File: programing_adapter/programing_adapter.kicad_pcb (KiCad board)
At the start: 2 copper layers, 87 x 98 mm, 72 parts, among them J1 Conn_02x05_SWD, J2 USB_A, SW1 SW_RESET

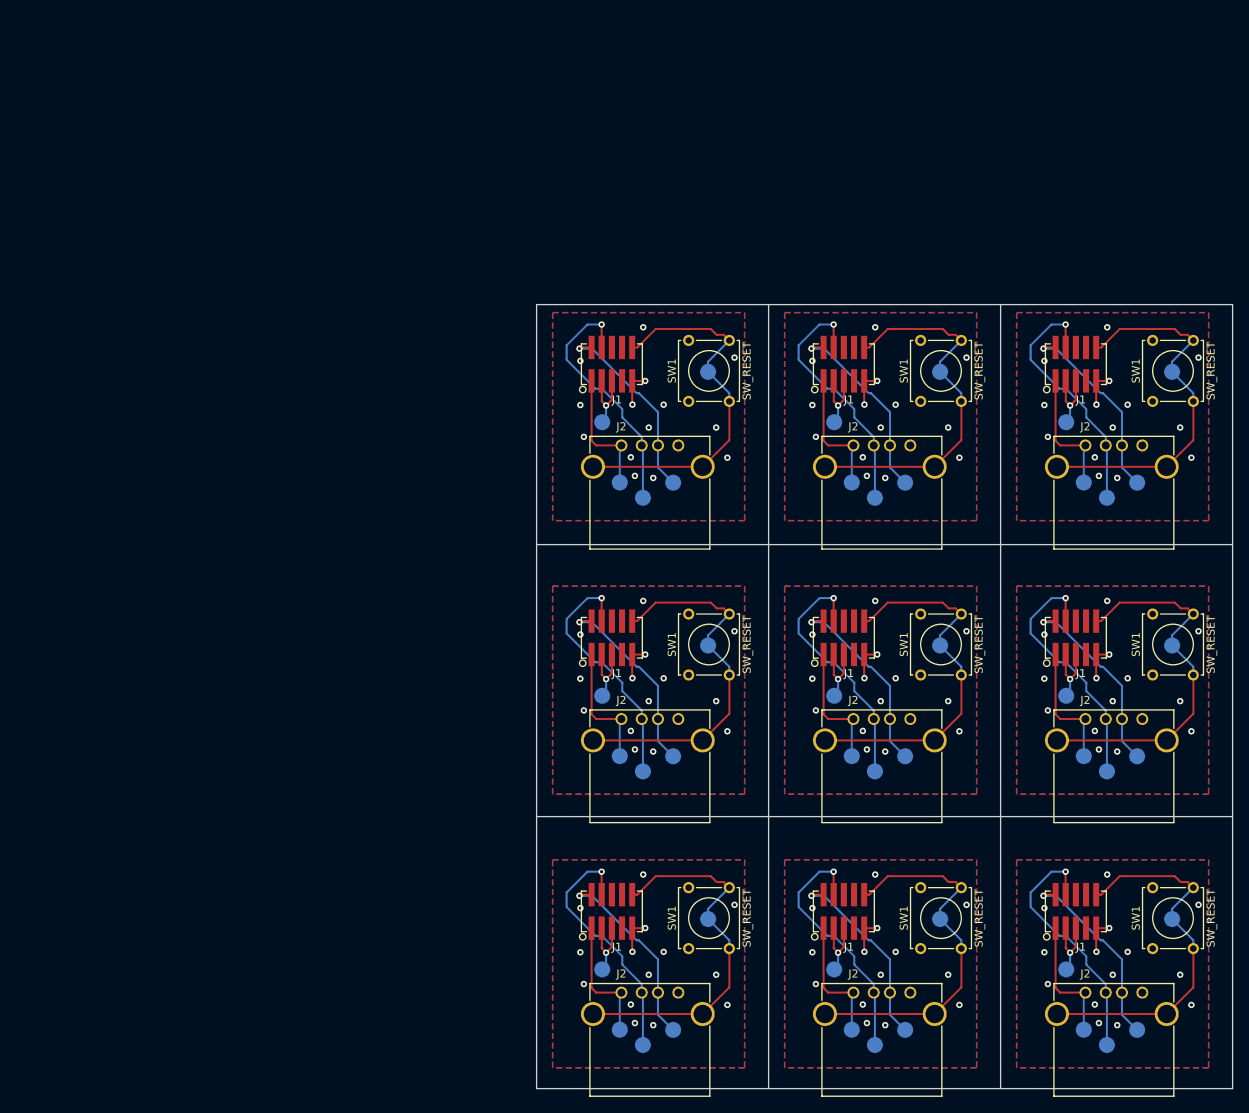
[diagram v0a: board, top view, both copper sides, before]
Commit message: remake programming adapter to be much more flexable
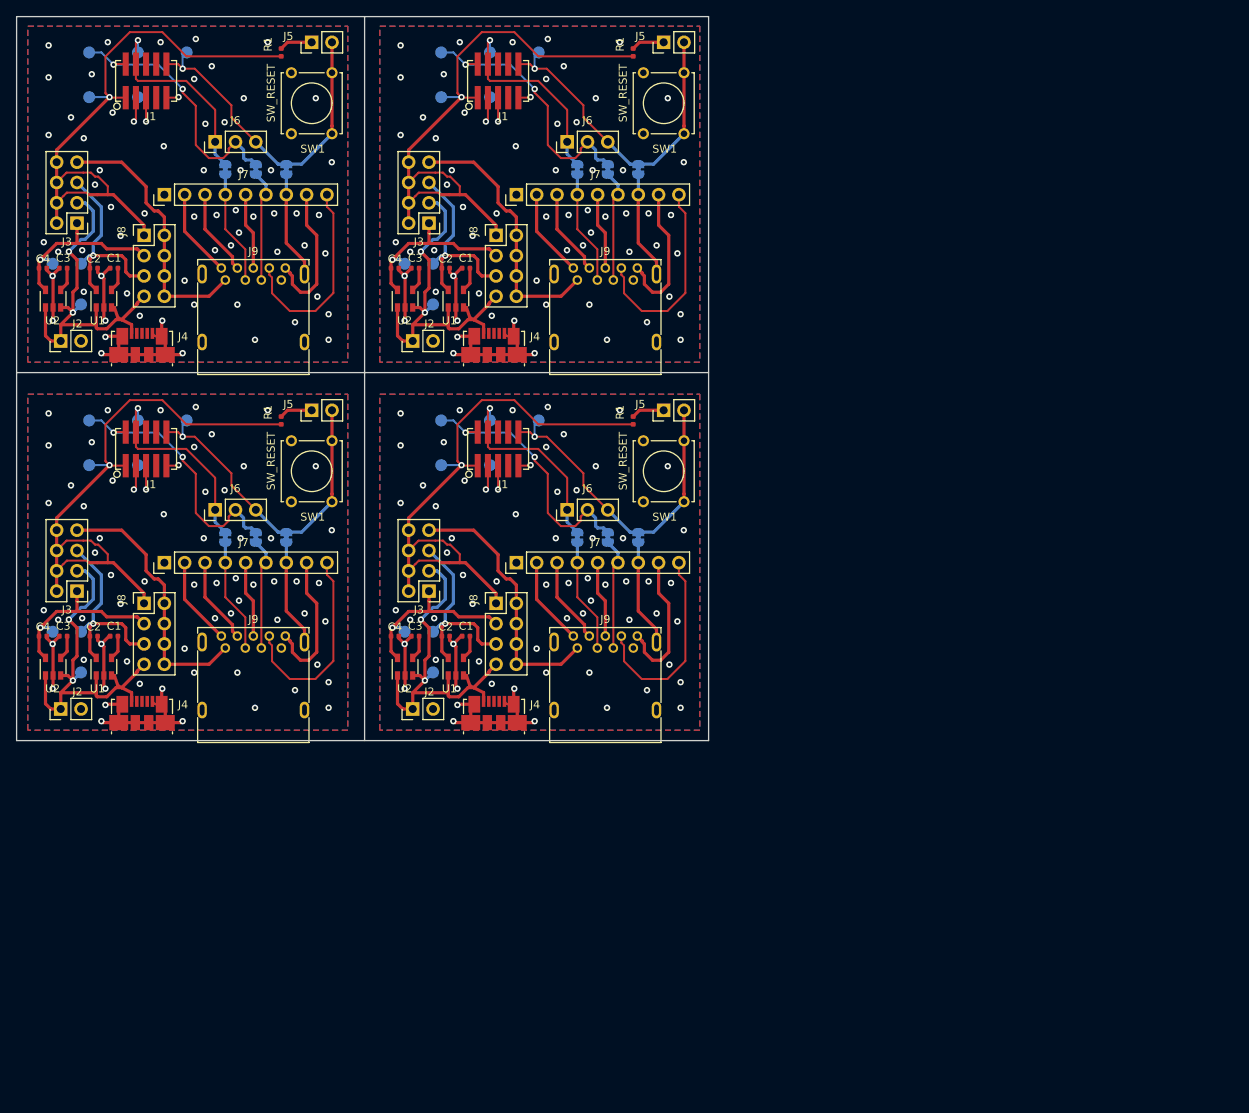
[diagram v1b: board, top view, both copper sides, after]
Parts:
- removed the J1 at (186.4, 148.8)
- removed the J1 at (157.4, 148.8)
- removed the J1 at (128.4, 148.8)
- removed the J1 at (186.4, 114.7)
- removed the J1 at (157.4, 114.7)
- removed the J1 at (128.4, 114.7)
- removed the J1 at (186.4, 80.5)
- removed the J1 at (157.4, 80.5)
- removed the J1 at (128.4, 80.5)
- removed the J2 at (187.6, 159.0)
- removed the J2 at (158.6, 159.0)
- removed the J2 at (129.6, 159.0)
- removed the J2 at (187.6, 124.8)
- removed the J2 at (158.6, 124.8)
- removed the J2 at (129.6, 124.8)
- removed the J2 at (187.6, 90.6)
- removed the J2 at (158.6, 90.6)
- removed the J2 at (129.6, 90.6)
- removed the SW1 at (196.0, 153.5)
- removed the SW1 at (167.0, 153.5)
- removed the SW1 at (138.0, 153.5)
- removed the SW1 at (196.0, 119.3)
- removed the SW1 at (167.0, 119.3)
- removed the SW1 at (138.0, 119.3)
- removed the SW1 at (196.0, 85.1)
- removed the SW1 at (167.0, 85.1)
- removed the SW1 at (138.0, 85.1)
- removed the TP1 at (187.4, 163.6)
- removed the TP1 at (158.4, 163.6)
- removed the TP1 at (129.4, 163.6)
- removed the TP1 at (187.4, 129.4)
- removed the TP1 at (158.4, 129.4)
- removed the TP1 at (129.4, 129.4)
- removed the TP1 at (187.4, 95.2)
- removed the TP1 at (158.4, 95.2)
- removed the TP1 at (129.4, 95.2)
- removed the TP2 at (185.2, 156.1)
- removed the TP2 at (156.2, 156.1)
- removed the TP2 at (127.2, 156.1)
- removed the TP2 at (185.2, 121.9)
- removed the TP2 at (156.2, 121.9)
- removed the TP2 at (127.2, 121.9)
- removed the TP2 at (185.2, 87.7)
- removed the TP2 at (156.2, 87.7)
- removed the TP2 at (127.2, 87.7)
- removed the TP3 at (194.1, 163.7)
- removed the TP3 at (165.1, 163.7)
- removed the TP3 at (136.1, 163.7)
- removed the TP3 at (194.1, 129.5)
- removed the TP3 at (165.1, 129.5)
- removed the TP3 at (136.1, 129.5)
- removed the TP3 at (194.1, 95.3)
- removed the TP3 at (165.1, 95.3)
- removed the TP3 at (136.1, 95.3)
- removed the TP4 at (190.3, 165.6)
- removed the TP4 at (161.3, 165.6)
- removed the TP4 at (132.3, 165.6)
- removed the TP4 at (190.3, 131.3)
- removed the TP4 at (161.3, 131.3)
- removed the TP4 at (132.3, 131.3)
- removed the TP4 at (190.3, 97.2)
- removed the TP4 at (161.3, 97.2)
- removed the TP4 at (132.3, 97.2)
- removed the TP5 at (198.4, 149.8)
- removed the TP5 at (169.4, 149.8)
- removed the TP5 at (140.4, 149.8)
- removed the TP5 at (198.4, 115.6)
- removed the TP5 at (169.4, 115.6)
- removed the TP5 at (140.4, 115.6)
- removed the TP5 at (198.4, 81.4)
- removed the TP5 at (169.4, 81.4)
- removed the TP5 at (140.4, 81.4)
- added C1: .1u, Capacitor_SMD:C_0402_1005Metric, F.Cu at (110.2, 114.4)
- added C1: .1u, Capacitor_SMD:C_0402_1005Metric, F.Cu at (66.2, 114.4)
- added C1: .1u, Capacitor_SMD:C_0402_1005Metric, F.Cu at (110.2, 68.4)
- added C1: .1u, Capacitor_SMD:C_0402_1005Metric, F.Cu at (66.2, 68.4)
- added C2: 4.7u, Capacitor_SMD:C_0402_1005Metric, F.Cu at (107.6, 114.4)
- added C2: 4.7u, Capacitor_SMD:C_0402_1005Metric, F.Cu at (63.6, 114.4)
- added C2: 4.7u, Capacitor_SMD:C_0402_1005Metric, F.Cu at (107.6, 68.4)
- added C2: 4.7u, Capacitor_SMD:C_0402_1005Metric, F.Cu at (63.6, 68.4)
- added C3: .1u, Capacitor_SMD:C_0402_1005Metric, F.Cu at (103.8, 114.4)
- added C3: .1u, Capacitor_SMD:C_0402_1005Metric, F.Cu at (59.8, 114.4)
- added C3: .1u, Capacitor_SMD:C_0402_1005Metric, F.Cu at (103.8, 68.4)
- added C3: .1u, Capacitor_SMD:C_0402_1005Metric, F.Cu at (59.8, 68.4)
- added C4: 4.7u, Capacitor_SMD:C_0402_1005Metric, F.Cu at (101.3, 114.4)
- added C4: 4.7u, Capacitor_SMD:C_0402_1005Metric, F.Cu at (57.3, 114.4)
- added C4: 4.7u, Capacitor_SMD:C_0402_1005Metric, F.Cu at (101.3, 68.4)
- added C4: 4.7u, Capacitor_SMD:C_0402_1005Metric, F.Cu at (57.3, 68.4)
- added J1: SWD, CustomKiCadLibrary:185G087, F.Cu at (114.2, 91.0)
- added J1: SWD, CustomKiCadLibrary:185G087, F.Cu at (70.2, 91.0)
- added J1: SWD, CustomKiCadLibrary:185G087, F.Cu at (114.2, 45.0)
- added J1: SWD, CustomKiCadLibrary:185G087, F.Cu at (70.2, 45.0)
- added J2: Vin, Connector_PinHeader_2.54mm:PinHeader_1x02_P2.54mm_Vertical, F.Cu at (103.5, 123.5)
- added J2: Vin, Connector_PinHeader_2.54mm:PinHeader_1x02_P2.54mm_Vertical, F.Cu at (59.5, 123.5)
- added J2: Vin, Connector_PinHeader_2.54mm:PinHeader_1x02_P2.54mm_Vertical, F.Cu at (103.5, 77.5)
- added J2: Vin, Connector_PinHeader_2.54mm:PinHeader_1x02_P2.54mm_Vertical, F.Cu at (59.5, 77.5)
- added J3: Set Prog V, Connector_PinHeader_2.54mm:PinHeader_2x04_P2.54mm_Vertical, F.Cu at (105.5, 108.8)
- added J3: Set Prog V, Connector_PinHeader_2.54mm:PinHeader_2x04_P2.54mm_Vertical, F.Cu at (61.5, 108.8)
- added J3: Set Prog V, Connector_PinHeader_2.54mm:PinHeader_2x04_P2.54mm_Vertical, F.Cu at (105.5, 62.8)
- added J3: Set Prog V, Connector_PinHeader_2.54mm:PinHeader_2x04_P2.54mm_Vertical, F.Cu at (61.5, 62.8)
- added J4: USB_B_Micro, Connector_USB:USB_Micro-B_Molex_47346-0001, F.Cu at (113.7, 124.1)
- added J4: USB_B_Micro, Connector_USB:USB_Micro-B_Molex_47346-0001, F.Cu at (69.7, 124.1)
- added J4: USB_B_Micro, Connector_USB:USB_Micro-B_Molex_47346-0001, F.Cu at (113.7, 78.1)
- added J4: USB_B_Micro, Connector_USB:USB_Micro-B_Molex_47346-0001, F.Cu at (69.7, 78.1)
- added J5: Conn_01x02, Connector_PinHeader_2.54mm:PinHeader_1x02_P2.54mm_Vertical, F.Cu at (134.9, 86.2)
- added J5: Conn_01x02, Connector_PinHeader_2.54mm:PinHeader_1x02_P2.54mm_Vertical, F.Cu at (90.9, 86.2)
- added J5: Conn_01x02, Connector_PinHeader_2.54mm:PinHeader_1x02_P2.54mm_Vertical, F.Cu at (134.9, 40.2)
- added J5: Conn_01x02, Connector_PinHeader_2.54mm:PinHeader_1x02_P2.54mm_Vertical, F.Cu at (90.9, 40.2)
- added J6: Conn_01x03, Connector_PinHeader_2.54mm:PinHeader_1x03_P2.54mm_Vertical, F.Cu at (122.8, 98.7)
- added J6: Conn_01x03, Connector_PinHeader_2.54mm:PinHeader_1x03_P2.54mm_Vertical, F.Cu at (78.8, 98.7)
- added J6: Conn_01x03, Connector_PinHeader_2.54mm:PinHeader_1x03_P2.54mm_Vertical, F.Cu at (122.8, 52.7)
- added J6: Conn_01x03, Connector_PinHeader_2.54mm:PinHeader_1x03_P2.54mm_Vertical, F.Cu at (78.8, 52.7)
- added J7: Conn_01x09, Connector_PinHeader_2.54mm:PinHeader_1x09_P2.54mm_Vertical, F.Cu at (116.5, 105.3)
- added J7: Conn_01x09, Connector_PinHeader_2.54mm:PinHeader_1x09_P2.54mm_Vertical, F.Cu at (72.5, 105.3)
- added J7: Conn_01x09, Connector_PinHeader_2.54mm:PinHeader_1x09_P2.54mm_Vertical, F.Cu at (116.5, 59.3)
- added J7: Conn_01x09, Connector_PinHeader_2.54mm:PinHeader_1x09_P2.54mm_Vertical, F.Cu at (72.5, 59.3)
- added J8: Set Target V, Connector_PinHeader_2.54mm:PinHeader_2x04_P2.54mm_Vertical, F.Cu at (113.9, 110.3)
- added J8: Set Target V, Connector_PinHeader_2.54mm:PinHeader_2x04_P2.54mm_Vertical, F.Cu at (69.9, 110.3)
- added J8: Set Target V, Connector_PinHeader_2.54mm:PinHeader_2x04_P2.54mm_Vertical, F.Cu at (113.9, 64.3)
- added J8: Set Target V, Connector_PinHeader_2.54mm:PinHeader_2x04_P2.54mm_Vertical, F.Cu at (69.9, 64.3)
- added J9: USB3_A, Connector_USB:USB3_A_Molex_48393-001, F.Cu at (124.1, 115.9)
- added J9: USB3_A, Connector_USB:USB3_A_Molex_48393-001, F.Cu at (80.1, 115.9)
- added J9: USB3_A, Connector_USB:USB3_A_Molex_48393-001, F.Cu at (124.1, 69.9)
- added J9: USB3_A, Connector_USB:USB3_A_Molex_48393-001, F.Cu at (80.1, 69.9)
- added JP1: SolderJumper_2_Bridged, Jumper:SolderJumper-2_P1.3mm_Bridged_RoundedPad1.0x1.5mm, B.Cu at (131.7, 102.1)
- added JP1: SolderJumper_2_Bridged, Jumper:SolderJumper-2_P1.3mm_Bridged_RoundedPad1.0x1.5mm, B.Cu at (87.7, 102.1)
- added JP1: SolderJumper_2_Bridged, Jumper:SolderJumper-2_P1.3mm_Bridged_RoundedPad1.0x1.5mm, B.Cu at (131.7, 56.1)
- added JP1: SolderJumper_2_Bridged, Jumper:SolderJumper-2_P1.3mm_Bridged_RoundedPad1.0x1.5mm, B.Cu at (87.7, 56.1)
- added JP2: SolderJumper_2_Bridged, Jumper:SolderJumper-2_P1.3mm_Bridged_RoundedPad1.0x1.5mm, B.Cu at (124.1, 102.1)
- added JP2: SolderJumper_2_Bridged, Jumper:SolderJumper-2_P1.3mm_Bridged_RoundedPad1.0x1.5mm, B.Cu at (80.1, 102.1)
- added JP2: SolderJumper_2_Bridged, Jumper:SolderJumper-2_P1.3mm_Bridged_RoundedPad1.0x1.5mm, B.Cu at (124.1, 56.1)
- added JP2: SolderJumper_2_Bridged, Jumper:SolderJumper-2_P1.3mm_Bridged_RoundedPad1.0x1.5mm, B.Cu at (80.1, 56.1)
- added JP3: SolderJumper_2_Bridged, Jumper:SolderJumper-2_P1.3mm_Bridged_RoundedPad1.0x1.5mm, B.Cu at (127.9, 102.1)
- added JP3: SolderJumper_2_Bridged, Jumper:SolderJumper-2_P1.3mm_Bridged_RoundedPad1.0x1.5mm, B.Cu at (83.9, 102.1)
- added JP3: SolderJumper_2_Bridged, Jumper:SolderJumper-2_P1.3mm_Bridged_RoundedPad1.0x1.5mm, B.Cu at (127.9, 56.1)
- added JP3: SolderJumper_2_Bridged, Jumper:SolderJumper-2_P1.3mm_Bridged_RoundedPad1.0x1.5mm, B.Cu at (83.9, 56.1)
- added R1: 10k, Resistor_SMD:R_0402_1005Metric, F.Cu at (131.1, 87.5)
- added R1: 10k, Resistor_SMD:R_0402_1005Metric, F.Cu at (87.1, 87.5)
- added R1: 10k, Resistor_SMD:R_0402_1005Metric, F.Cu at (131.1, 41.5)
- added R1: 10k, Resistor_SMD:R_0402_1005Metric, F.Cu at (87.1, 41.5)
- added SW1: SW_RESET, Buttons_Switches_THT:SW_Tactile_Straight_KSA0Axx1LFTR, F.Cu at (132.3, 97.6)
- added SW1: SW_RESET, Buttons_Switches_THT:SW_Tactile_Straight_KSA0Axx1LFTR, F.Cu at (88.3, 97.6)
- added SW1: SW_RESET, Buttons_Switches_THT:SW_Tactile_Straight_KSA0Axx1LFTR, F.Cu at (132.3, 51.6)
- added SW1: SW_RESET, Buttons_Switches_THT:SW_Tactile_Straight_KSA0Axx1LFTR, F.Cu at (88.3, 51.6)
- added TP1: 1V8, TestPoint:TestPoint_Pad_D1.5mm, B.Cu at (102.5, 113.9)
- added TP1: 1V8, TestPoint:TestPoint_Pad_D1.5mm, B.Cu at (58.5, 113.9)
- added TP1: 1V8, TestPoint:TestPoint_Pad_D1.5mm, B.Cu at (102.5, 67.9)
- added TP1: 1V8, TestPoint:TestPoint_Pad_D1.5mm, B.Cu at (58.5, 67.9)
- added TP2: GND, TestPoint:TestPoint_Pad_D1.5mm, B.Cu at (113.2, 93.1)
- added TP2: GND, TestPoint:TestPoint_Pad_D1.5mm, B.Cu at (69.2, 93.1)
- added TP2: GND, TestPoint:TestPoint_Pad_D1.5mm, B.Cu at (113.2, 47.1)
- added TP2: GND, TestPoint:TestPoint_Pad_D1.5mm, B.Cu at (69.2, 47.1)
- added TP3: SWDIO, TestPoint:TestPoint_Pad_D1.5mm, B.Cu at (107.1, 87.5)
- added TP3: SWDIO, TestPoint:TestPoint_Pad_D1.5mm, B.Cu at (63.1, 87.5)
- added TP3: SWDIO, TestPoint:TestPoint_Pad_D1.5mm, B.Cu at (107.1, 41.5)
- added TP3: SWDIO, TestPoint:TestPoint_Pad_D1.5mm, B.Cu at (63.1, 41.5)
- added TP4: SWDCLK, TestPoint:TestPoint_Pad_D1.5mm, B.Cu at (113.2, 87.5)
- added TP4: SWDCLK, TestPoint:TestPoint_Pad_D1.5mm, B.Cu at (69.2, 87.5)
- added TP4: SWDCLK, TestPoint:TestPoint_Pad_D1.5mm, B.Cu at (113.2, 41.5)
- added TP4: SWDCLK, TestPoint:TestPoint_Pad_D1.5mm, B.Cu at (69.2, 41.5)
- added TP5: Reset, TestPoint:TestPoint_Pad_D1.5mm, B.Cu at (119.3, 87.5)
- added TP5: Reset, TestPoint:TestPoint_Pad_D1.5mm, B.Cu at (75.3, 87.5)
- added TP5: Reset, TestPoint:TestPoint_Pad_D1.5mm, B.Cu at (119.3, 41.5)
- added TP5: Reset, TestPoint:TestPoint_Pad_D1.5mm, B.Cu at (75.3, 41.5)
- added TP6: 3V3, TestPoint:TestPoint_Pad_D1.5mm, B.Cu at (106.1, 113.9)
- added TP6: 3V3, TestPoint:TestPoint_Pad_D1.5mm, B.Cu at (62.1, 113.9)
- added TP6: 3V3, TestPoint:TestPoint_Pad_D1.5mm, B.Cu at (106.1, 67.9)
- added TP6: 3V3, TestPoint:TestPoint_Pad_D1.5mm, B.Cu at (62.1, 67.9)
- added TP7: VProg, TestPoint:TestPoint_Pad_D1.5mm, B.Cu at (107.1, 93.1)
- added TP7: VProg, TestPoint:TestPoint_Pad_D1.5mm, B.Cu at (63.1, 93.1)
- added TP7: VProg, TestPoint:TestPoint_Pad_D1.5mm, B.Cu at (107.1, 47.1)
- added TP7: VProg, TestPoint:TestPoint_Pad_D1.5mm, B.Cu at (63.1, 47.1)
- added TP8: 5V, TestPoint:TestPoint_Pad_D1.5mm, B.Cu at (106.1, 119.0)
- added TP8: 5V, TestPoint:TestPoint_Pad_D1.5mm, B.Cu at (62.1, 119.0)
- added TP8: 5V, TestPoint:TestPoint_Pad_D1.5mm, B.Cu at (106.1, 73.0)
- added TP8: 5V, TestPoint:TestPoint_Pad_D1.5mm, B.Cu at (62.1, 73.0)
- added U1: AP131-33, Package_TO_SOT_SMD:SOT-23-5, F.Cu at (108.9, 118.3)
- added U1: AP131-33, Package_TO_SOT_SMD:SOT-23-5, F.Cu at (64.9, 118.3)
- added U1: AP131-33, Package_TO_SOT_SMD:SOT-23-5, F.Cu at (108.9, 72.3)
- added U1: AP131-33, Package_TO_SOT_SMD:SOT-23-5, F.Cu at (64.9, 72.3)
- added U2: AP131-18, Package_TO_SOT_SMD:SOT-23-5, F.Cu at (102.6, 118.3)
- added U2: AP131-18, Package_TO_SOT_SMD:SOT-23-5, F.Cu at (58.6, 118.3)
- added U2: AP131-18, Package_TO_SOT_SMD:SOT-23-5, F.Cu at (102.6, 72.3)
- added U2: AP131-18, Package_TO_SOT_SMD:SOT-23-5, F.Cu at (58.6, 72.3)
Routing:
- net /VProg: track 0.00 -> 303.7 mm, vias 0 -> 4
- net /Reset: track 421.0 -> 168.1 mm, vias 0 -> 4
- net /SWDCLK: track 286.2 -> 101.2 mm, vias 9 -> 4
- net /VTarg: track 0.00 -> 133.3 mm
- net +3V3: track 0.00 -> 103.4 mm, vias 0 -> 4
- net Net-(J7-Pad9): track 0.00 -> 101.8 mm
- net +1V8: track 0.00 -> 91.5 mm, vias 0 -> 4
- net /SWDIO: track 218.4 -> 135.5 mm, vias 9 -> 8
- net Net-(J7-Pad8): track 0.00 -> 71.9 mm
- net GND: track 121.9 -> 180.2 mm, vias 135 -> 260
- net Net-(J7-Pad4): track 0.00 -> 56.9 mm
- net Net-(J7-Pad6): track 0.00 -> 55.8 mm
- net +5V: track 145.5 -> 199.9 mm, vias 0 -> 8
- net Net-(J7-Pad7): track 0.00 -> 53.5 mm
- net Net-(J7-Pad2): track 0.00 -> 44.3 mm
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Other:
- board size 87 x 98 mm -> 86.5 x 90.5 mm
- rule trace_min: 0.1524 -> 0.2
- board text added: "V Score"
